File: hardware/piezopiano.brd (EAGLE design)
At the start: 175.5 x 99.8 mm, 73 parts, among them J1 CON2, J4 JST-PH-2-SMT-SE, Q1 DMN3404L, Q2 DMN3404L, Q3 DMN3404L, Q4 DMN3404L, Q5 DMN3404L, Q6 DMN3404L, Q7 DMN3404L, Q8 DMN3404L, U2 CH340E_MSOP10, U3 TP4333, U4 MEGA328PB-AU, Y1 830069392

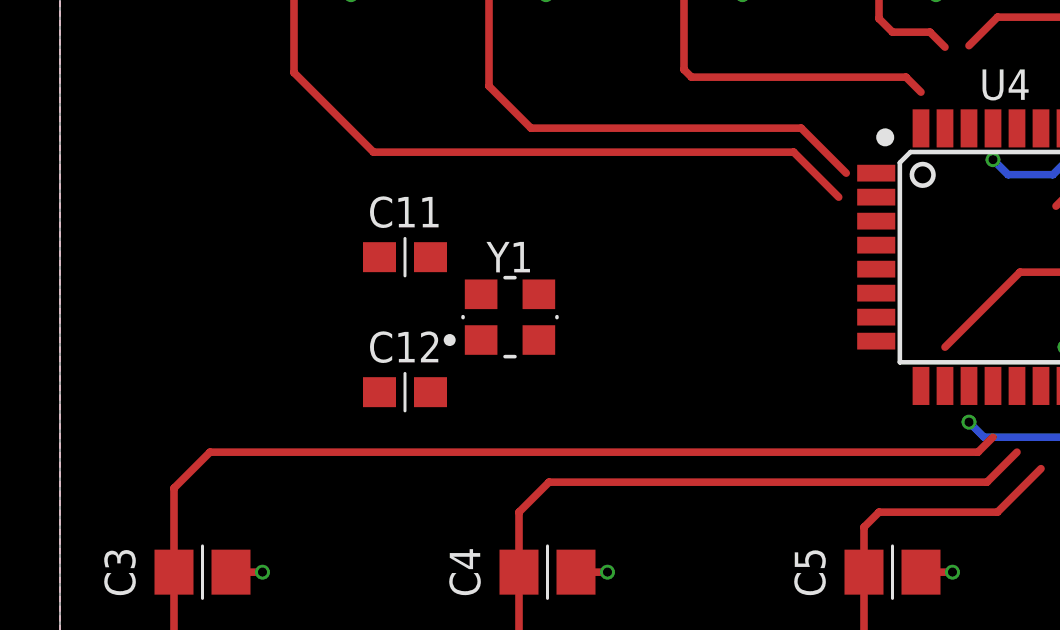
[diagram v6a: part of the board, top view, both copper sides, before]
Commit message: Added RGB LED
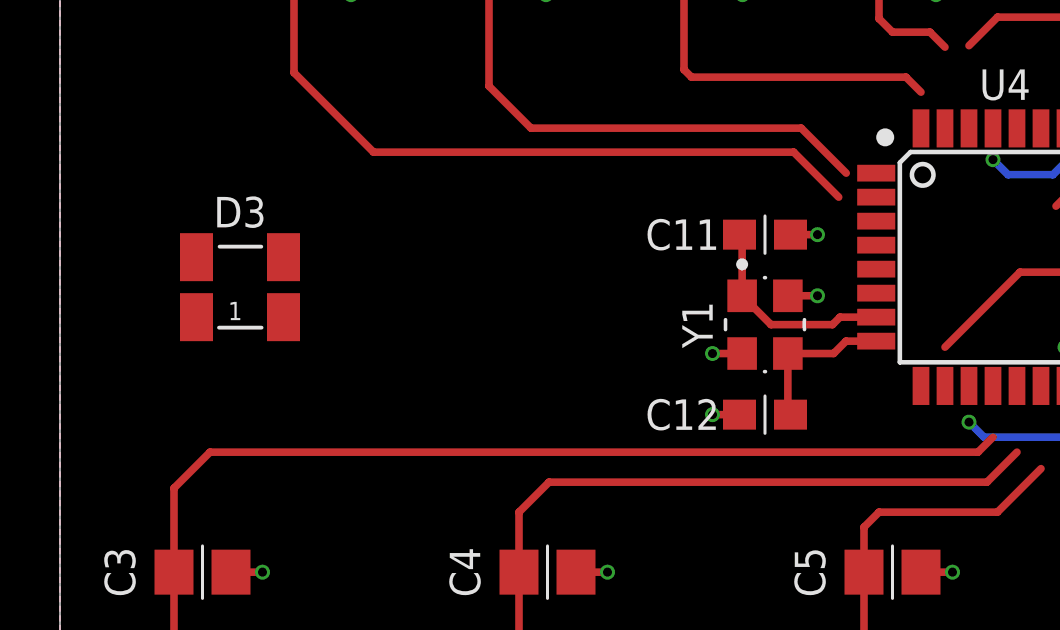
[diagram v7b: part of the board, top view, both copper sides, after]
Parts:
- added D3: (no value), zaan-Optoelectronics:WL-SFCX_1210
- moved C11 12.0 mm to (23.5, 28.2)
- moved C12 12.0 mm to (23.5, 22.2), turned to 180 degrees
- moved Y1 8.50 mm to (23.5, 25.2), turned to 270 degrees
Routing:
- net XTAL1: track 0.00 -> 7.05 mm
- net XTAL2: track 0.00 -> 5.19 mm
- net GND: track 39.2 -> 42.9 mm, vias 33 -> 37

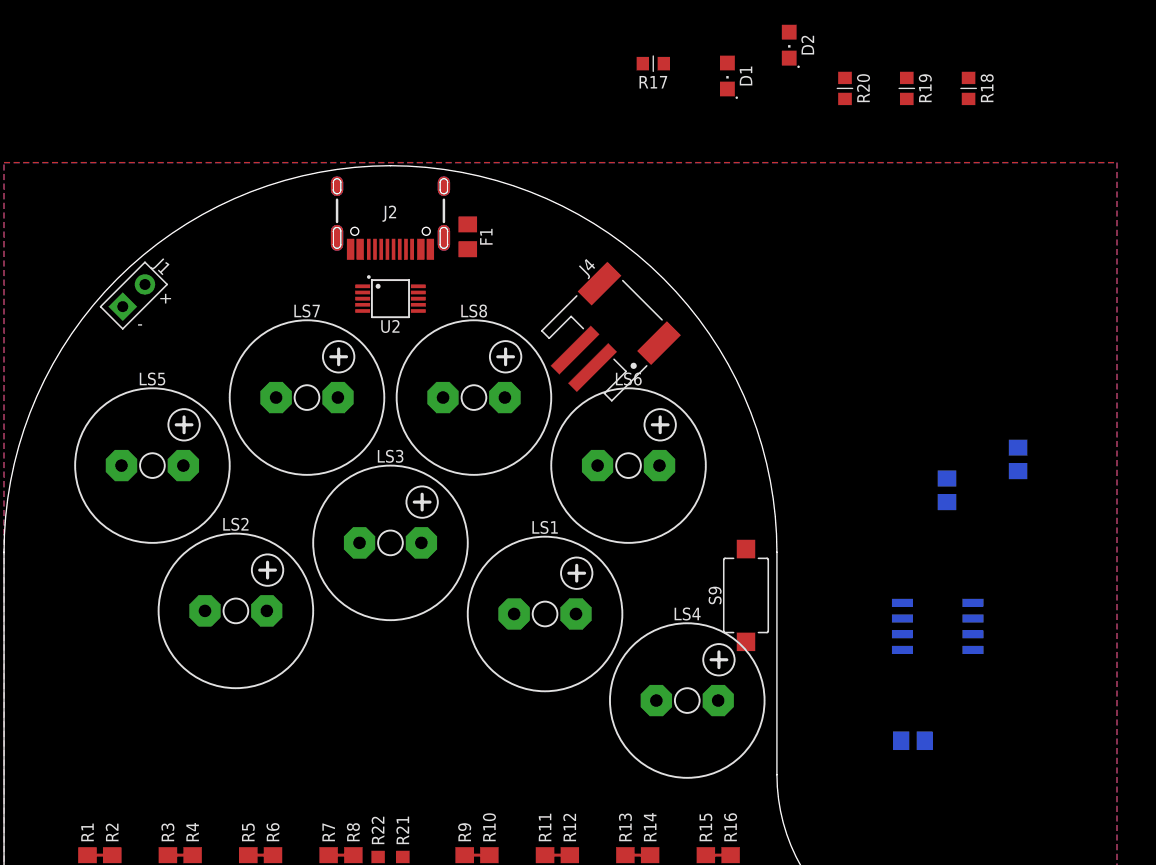
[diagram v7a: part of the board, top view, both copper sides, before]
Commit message: Added inductor, corrected LED
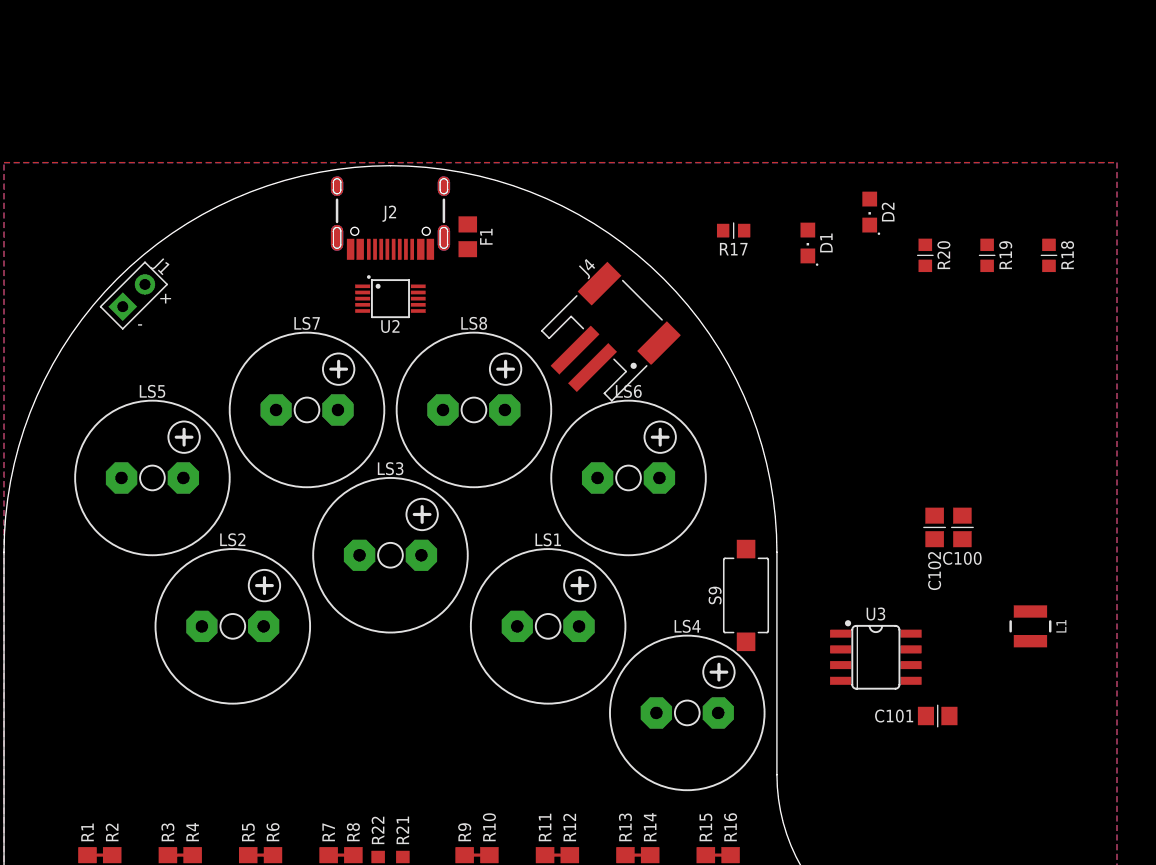
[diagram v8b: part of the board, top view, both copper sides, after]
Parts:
- added L1: 1.5u, zaan-Inductors:WE-LQS_3015
- moved D1 15.0 mm to (65.0, 93.5)
- moved D2 15.0 mm to (70.0, 96.0)
- moved R17 15.0 mm to (59.0, 94.5)
- moved R18 15.0 mm to (84.5, 92.5)
- moved R19 15.0 mm to (79.5, 92.5)
- moved R20 15.0 mm to (74.5, 92.5)
- moved C100 7.11 mm to (77.5, 70.5), flipped to the top
- moved U3 5.59 mm to (70.5, 60.0), flipped to the top
- moved C102 3.16 mm to (75.2, 70.5), flipped to the top
- moved C101 2.83 mm to (75.5, 55.2), flipped to the top
- moved LS2 1.27 mm to (18.5, 62.5)
- moved LS1 1.03 mm to (44.0, 62.5)
- moved LS3 1.00 mm to (31.2, 68.2)
- moved LS4 1.00 mm to (55.2, 55.5)
- moved LS5 1.00 mm to (12.0, 74.5)
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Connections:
- net N$21: now also L1.1
- net N$22: now also L1.2
